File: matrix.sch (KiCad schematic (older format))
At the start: 135 parts

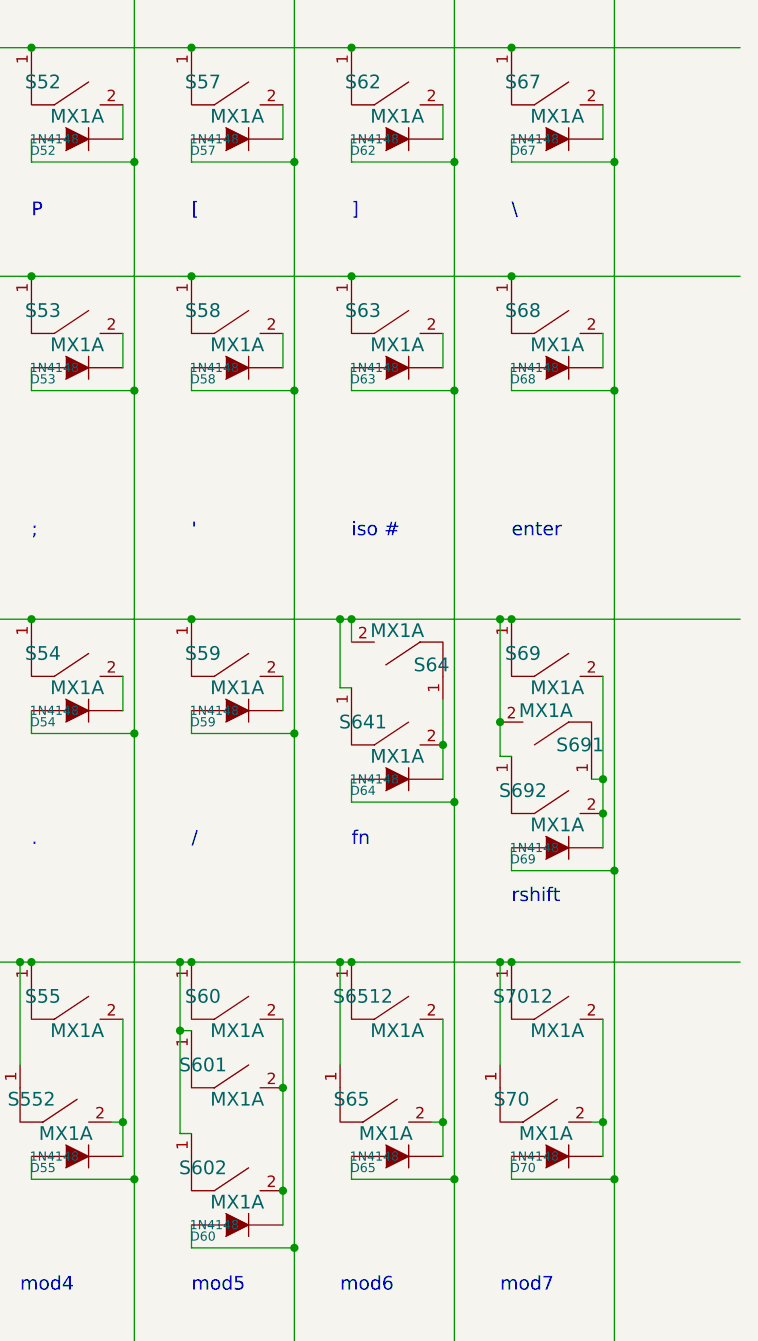
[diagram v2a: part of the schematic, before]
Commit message: Remove old layout around rswitch
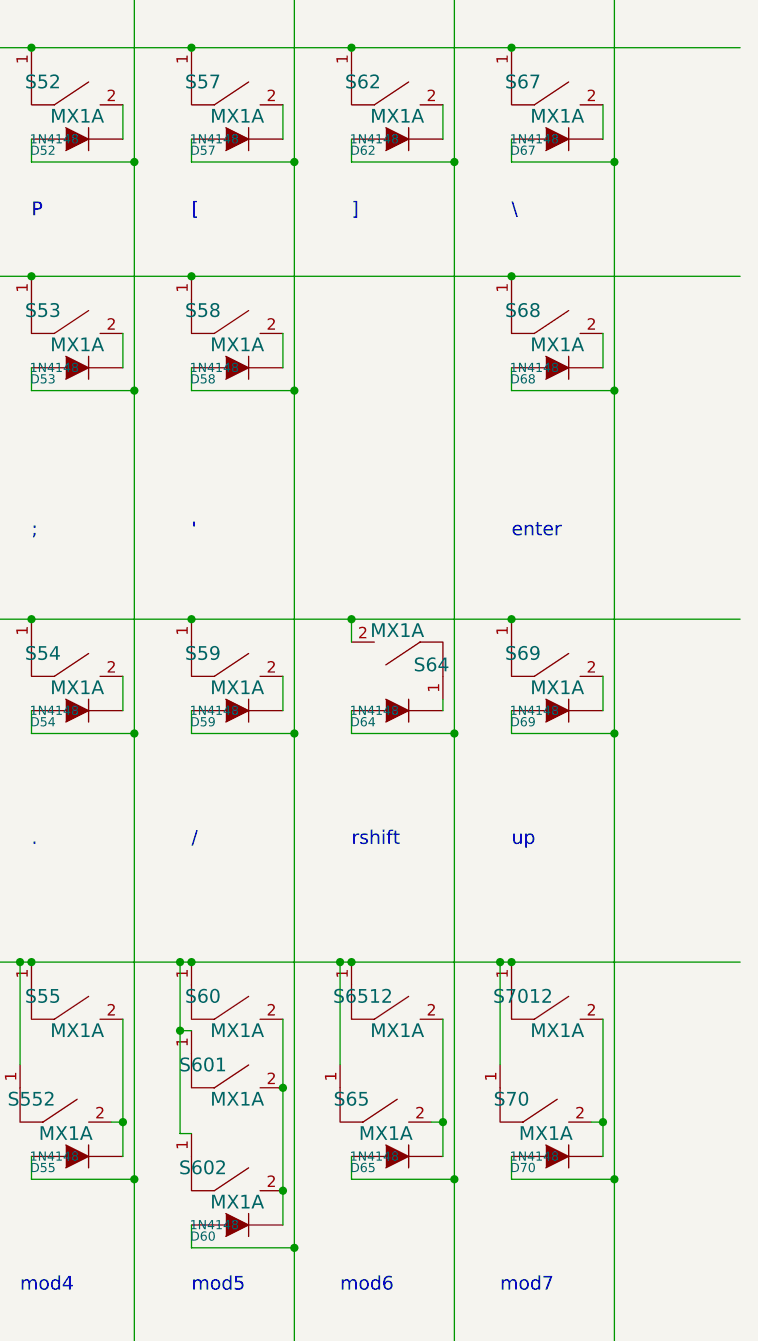
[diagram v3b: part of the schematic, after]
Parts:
- removed D63: 1N4148, 0805:0805D, symbol device:DIODE
- removed S63, S641, S691, S692: MX1A, mx1a:MX1A_no3d, symbol mx1a-simple:MX1A
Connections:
- wire segments 370 -> 354
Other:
- note added: "up"
- note removed: "fn"
- note removed: "iso #"
- moved on the sheet: D64, D69
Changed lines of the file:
@@
-$EndComp
-$Comp
-L mx1a-simple:MX1A S63
-U 1 1 5040DE9F
-P 11750 5550
-F 0 "S63" H 11600 5800 60  0000 C CNN
-F 1 "MX1A" H 11750 5650 60  0000 C CNN
-F 2 "mx1a:MX1A_no3d" H 11750 5550 60  0001 C CNN
-F 3 "" H 11750 5550 60  0001 C CNN
-	1    11750 5550
-	1    0    0    -1
 $EndComp
 $Comp
@@
 F 3 "" H 12400 9000 60  0001 C CNN
 	1    12400 9000
-	1    0    0    -1
-$EndComp
-$Comp
-L mx1a-simple:MX1A S641
-U 1 1 5040E2D0
-P 11750 7350
-F 0 "S641" H 11600 7600 60  0000 C CNN
-F 1 "MX1A" H 11750 7450 60  0000 C CNN
-F 2 "mx1a:MX1A_no3d" H 11750 7350 60  0001 C CNN
-F 3 "" H 11750 7350 60  0001 C CNN
-	1    11750 7350
 	1    0    0    -1
 $EndComp
@@
 $EndComp
 $Comp
-L mx1a-simple:MX1A S691
-U 1 1 5051FE50
-P 12400 6950
-F 0 "S691" H 12250 7200 60  0000 C CNN
-F 1 "MX1A" H 12400 7050 60  0000 C CNN
-F 2 "mx1a:MX1A_no3d" H 12400 6950 60  0001 C CNN
-F 3 "" H 12400 6950 60  0001 C CNN
-	1    12400 6950
-	-1   0    0    1
-$EndComp
-$Comp
-L mx1a-simple:MX1A S692
-U 1 1 5051FE56
-P 12450 7650
-F 0 "S692" H 12300 7900 60  0000 C CNN
-F 1 "MX1A" H 12450 7750 60  0000 C CNN
-F 2 "mx1a:MX1A_no3d" H 12450 7650 60  0001 C CNN
-F 3 "" H 12450 7650 60  0001 C CNN
-	1    12450 7650
-	1    0    0    -1
-$EndComp
-$Comp
 L device:DIODE D06
 U 1 1 506B1C22
@@
 L device:DIODE D64
 U 1 1 506B59D7
-P 11750 7350
-F 0 "D64" H 11600 7300 40  0000 C CNN
-F 1 "1N4148" H 11650 7350 40  0000 C CNN
-F 2 "0805:0805D" H 11750 7350 60  0001 C CNN
-F 3 "" H 11750 7350 60  0001 C CNN
-F 4 "DC Components" H 5150 4750 60  0001 C CNN "Vendor"
-F 5 "CD4148WS(0805C)" H 5150 4750 60  0001 C CNN "Product"
-F 6 "TME" H 5150 4750 60  0001 C CNN "Supplier"
-F 7 "1N4148-0805" H 5150 4750 60  0001 C CNN "Supplier Symbol"
-	1    11750 7350
+P 11750 7050
+F 0 "D64" H 11600 7000 40  0000 C CNN
+F 1 "1N4148" H 11650 7050 40  0000 C CNN
+F 2 "0805:0805D" H 11750 7050 60  0001 C CNN
+F 3 "" H 11750 7050 60  0001 C CNN
+F 4 "DC Components" H 5150 4450 60  0001 C CNN "Vendor"
+F 5 "CD4148WS(0805C)" H 5150 4450 60  0001 C CNN "Product"
+F 6 "TME" H 5150 4450 60  0001 C CNN "Supplier"
+F 7 "1N4148-0805" H 5150 4450 60  0001 C CNN "Supplier Symbol"
+	1    11750 7050
 	1    0    0    -1
 $EndComp
@@
 L device:DIODE D69
 U 1 1 506B59E0
-P 12450 7650
-F 0 "D69" H 12300 7600 40  0000 C CNN
-F 1 "1N4148" H 12350 7650 40  0000 C CNN
-F 2 "0805:0805D" H 12450 7650 60  0001 C CNN
-F 3 "" H 12450 7650 60  0001 C CNN
-F 4 "DC Components" H 5300 4750 60  0001 C CNN "Vendor"
-F 5 "CD4148WS(0805C)" H 5300 4750 60  0001 C CNN "Product"
-F 6 "TME" H 5300 4750 60  0001 C CNN "Supplier"
-F 7 "1N4148-0805" H 5300 4750 60  0001 C CNN "Supplier Symbol"
-	1    12450 7650
+P 12450 7050
+F 0 "D69" H 12300 7000 40  0000 C CNN
+F 1 "1N4148" H 12350 7050 40  0000 C CNN
+F 2 "0805:0805D" H 12450 7050 60  0001 C CNN
+F 3 "" H 12450 7050 60  0001 C CNN
+F 4 "DC Components" H 5300 4150 60  0001 C CNN "Vendor"
+F 5 "CD4148WS(0805C)" H 5300 4150 60  0001 C CNN "Product"
+F 6 "TME" H 5300 4150 60  0001 C CNN "Supplier"
+F 7 "1N4148-0805" H 5300 4150 60  0001 C CNN "Supplier Symbol"
+	1    12450 7050
 	1    0    0    -1
 $EndComp
@@
 F 7 "1N4148-0805" H 5300 4050 60  0001 C CNN "Supplier Symbol"
 	1    12450 5550
-	1    0    0    -1
-$EndComp
-$Comp
-L device:DIODE D63
-U 1 1 506B5A1F
-P 11750 5550
-F 0 "D63" H 11600 5500 40  0000 C CNN
-F 1 "1N4148" H 11650 5550 40  0000 C CNN
-F 2 "0805:0805D" H 11750 5550 60  0001 C CNN
-F 3 "" H 11750 5550 60  0001 C CNN
-F 4 "DC Components" H 5150 4350 60  0001 C CNN "Vendor"
-F 5 "CD4148WS(0805C)" H 5150 4350 60  0001 C CNN "Product"
-F 6 "TME" H 5150 4350 60  0001 C CNN "Supplier"
-F 7 "1N4148-0805" H 5150 4350 60  0001 C CNN "Supplier Symbol"
-	1    11750 5550
 	1    0    0    -1
 $EndComp
@@
 Text Notes 10850 6300 0    60   ~ 0
 '
-Text Notes 11550 6300 0    60   ~ 0
-iso #
 Text Notes 12250 6300 0    60   ~ 0
 enter
@@
 /
 Text Notes 11550 7650 0    60   ~ 0
-fn
-Text Notes 12250 7900 0    60   ~ 0
 rshift
+Text Notes 12250 7650 0    60   ~ 0
+up
 Text Notes 3100 9600 0    60   ~ 0
 mod1
@@
 Connection ~ 10150 5150
 Connection ~ 10850 5150
-Connection ~ 11550 5150
 Connection ~ 12250 5150
 Connection ~ 12250 4150
@@
 	12000 1400 12000 3450
 Wire Wire Line
-	11500 6650 11500 6950
-Wire Wire Line
-	11500 6950 11550 6950
-Connection ~ 11500 6650
-Wire Wire Line
-	11950 7000 11950 7200
-Wire Wire Line
 	10550 8850 10500 8850
 Wire Wire Line
@@
 	12650 8850 12600 8850
 Wire Wire Line
-	12200 6650 12200 7100
-Connection ~ 12200 6650
-Wire Wire Line
-	12200 7250 12250 7250
-Wire Wire Line
-	12650 6900 12650 7350
+	12650 6900 12650 7050
 Wire Wire Line
 	3850 3350 3850 3450
@@
 	11250 7050 11250 6900
 Wire Wire Line
-	11550 7350 11550 7450
-Wire Wire Line
-	11550 7450 12000 7450
-Wire Wire Line
-	12250 7650 12250 7750
-Wire Wire Line
-	12250 7750 12700 7750
+	11550 7050 11550 7150
+Wire Wire Line
+	11550 7150 12000 7150
+Wire Wire Line
+	12250 7050 12250 7150
+Wire Wire Line
+	12250 7150 12700 7150
 Wire Wire Line
 	12250 9000 12250 9100
@@
 Wire Wire Line
 	12250 5650 12700 5650
-Wire Wire Line
-	11550 5550 11550 5650
-Wire Wire Line
-	11550 5650 12000 5650
-Wire Wire Line
-	11950 5550 11950 5400
 Wire Wire Line
 	10850 5550 10850 5650
@@
 Connection ~ 10600 5650
 Connection ~ 11300 5650
-Connection ~ 12000 5650
 Connection ~ 12700 9100
-Connection ~ 12700 7750
-Connection ~ 12000 7450
 Connection ~ 12000 9100
 Connection ~ 11300 9400
@@
 Connection ~ 9900 7150
 Connection ~ 9200 7150
-Connection ~ 11950 7200
 Connection ~ 9450 5150
 Connection ~ 9450 4150
 Connection ~ 9450 2950
-Connection ~ 12650 7500
 Wire Wire Line
 	11550 6750 11550 6650
@@
 	12250 3450 12250 3350
 Wire Wire Line
-	12600 7350 12650 7350
-Connection ~ 12650 7350
-Connection ~ 12200 7100
-Wire Wire Line
 	10100 8150 10150 8150
 Wire Wire Line
@@
 	12250 6650 13250 6650
 Wire Wire Line
-	10850 6650 11500 6650
-Wire Wire Line
-	11550 6650 12200 6650
-Wire Wire Line
 	10150 6650 10850 6650
 Wire Wire Line
@@
 	10150 5150 10850 5150
 Wire Wire Line
-	10850 5150 11550 5150
-Wire Wire Line
 	12250 5150 13250 5150
 Wire Wire Line
@@
 	11250 8700 11250 9150
 Wire Wire Line
-	11500 6650 11550 6650
-Wire Wire Line
-	12200 6650 12250 6650
-Wire Wire Line
 	5250 2950 5950 2950
 Wire Wire Line
@@
 	12700 4650 12700 5650
 Wire Wire Line
-	12000 4650 12000 5650
-Wire Wire Line
 	11300 4650 11300 5650
 Wire Wire Line
@@
 	11300 5650 11300 7150
 Wire Wire Line
-	12000 5650 12000 7450
-Wire Wire Line
 	12700 9100 12700 10000
 Wire Wire Line
-	12700 7750 12700 9100
-Wire Wire Line
-	12000 7450 12000 9100
-Wire Wire Line
 	12000 9100 12000 10000
 Wire Wire Line
@@
 	9200 7150 9200 10000
 Wire Wire Line
-	11950 7200 11950 7350
-Wire Wire Line
 	9450 5150 10150 5150
 Wire Wire Line
@@
 Wire Wire Line
 	9450 2950 10150 2950
-Wire Wire Line
-	12650 7500 12650 7650
-Wire Wire Line
-	12650 7350 12650 7500
-Wire Wire Line
-	12200 7100 12200 7250
 Wire Wire Line
 	9900 7150 9900 10000
@@
 Wire Wire Line
 	12650 5400 12650 5550
-Wire Wire Line
-	11550 5150 12250 5150
 Connection ~ 12700 5650
 Wire Wire Line
-	12700 5650 12700 7750
+	12700 5650 12700 7150
 Wire Wire Line
 	12250 5550 12250 5650
+Wire Wire Line
+	11950 7000 11950 7050
+Wire Wire Line
+	10850 6650 11550 6650
+Connection ~ 12000 7150
+Wire Wire Line
+	12000 7150 12000 9100
+Wire Wire Line
+	11550 6650 12250 6650
+Connection ~ 12700 7150
+Wire Wire Line
+	12700 7150 12700 9100
+Wire Wire Line
+	10850 5150 12250 5150
+Wire Wire Line
+	12000 4650 12000 7150
 $EndSCHEMATC

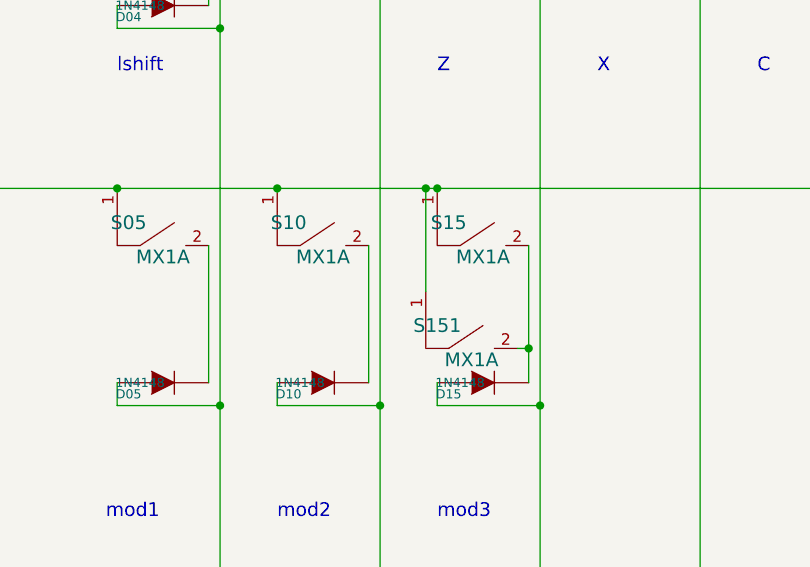
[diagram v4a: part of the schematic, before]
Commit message: Remove leds from PCB
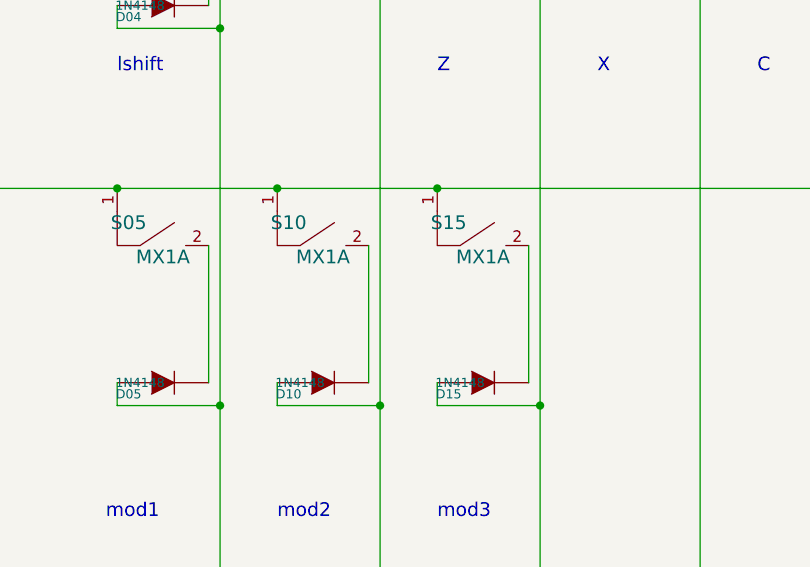
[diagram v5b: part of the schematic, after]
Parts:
- removed S151: MX1A, mx1a:MX1A_no3d, symbol mx1a-simple:MX1A
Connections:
- wire segments 354 -> 350
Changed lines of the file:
@@
 	4300 9100 4300 10000
-Wire Wire Line
-	4950 8850 4950 9000
-Wire Wire Line
-	4950 8400 4950 8850
-Connection ~ 4950 8850
-Wire Wire Line
-	4950 8850 4900 8850
-Wire Wire Line
-	3850 8150 4500 8150
-Wire Wire Line
-	4500 8150 4550 8150
-Connection ~ 4500 8150
-Wire Wire Line
-	4500 8150 4500 8600
-$Comp
-L mx1a-simple:MX1A S151
-U 1 1 5040F14F
-P 4700 9000
-F 0 "S151" H 4550 9250 60  0000 C CNN
-F 1 "MX1A" H 4700 9100 60  0000 C CNN
-F 2 "mx1a:MX1A_no3d" H 4700 9000 60  0001 C CNN
-F 3 "" H 4700 9000 60  0001 C CNN
-	1    4700 9000
-	1    0    0    -1
-$EndComp
 Wire Wire Line
 	1800 5150 3150 5150
@@
 Wire Wire Line
 	12000 4650 12000 7150
+Wire Wire Line
+	3850 8150 4550 8150
+Wire Wire Line
+	4950 8400 4950 9000
 $EndSCHEMATC

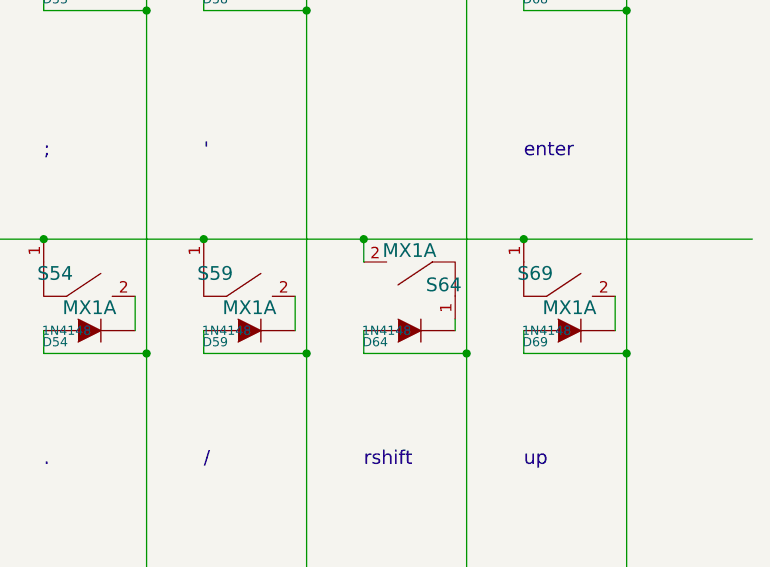
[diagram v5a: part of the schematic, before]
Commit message: Add rswitch and up buttons
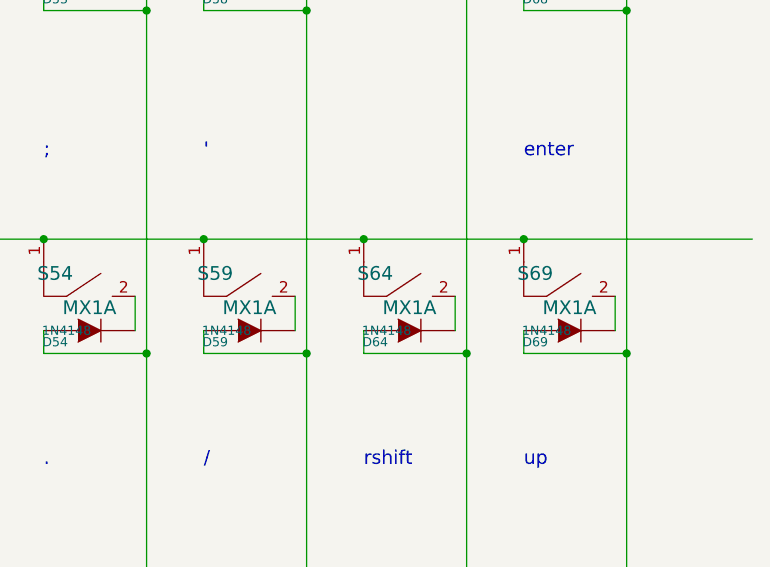
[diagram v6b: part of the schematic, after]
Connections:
- wire segments 350 -> 349
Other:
- moved on the sheet: S64
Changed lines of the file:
@@
-$EndComp
-$Comp
-L mx1a-simple:MX1A S64
-U 1 1 5040DEFF
-P 11750 6600
-F 0 "S64" H 11600 6850 60  0000 C CNN
-F 1 "MX1A" H 11750 6700 60  0000 C CNN
-F 2 "mx1a:MX1A_no3d" H 11750 6600 60  0001 C CNN
-F 3 "" H 11750 6600 60  0001 C CNN
-	1    11750 6600
-	-1   0    0    1
 $EndComp
 $Comp
@@
 Connection ~ 12250 6650
 Connection ~ 10850 6650
-Connection ~ 11550 6650
 Connection ~ 10150 6650
 Connection ~ 6650 6650
@@
 Connection ~ 9450 2950
 Wire Wire Line
-	11550 6750 11550 6650
-Wire Wire Line
 	10800 8900 10850 8900
 Wire Wire Line
@@
 Wire Wire Line
 	12250 5550 12250 5650
-Wire Wire Line
-	11950 7000 11950 7050
+Connection ~ 12000 7150
+Wire Wire Line
+	12000 7150 12000 9100
+Connection ~ 12700 7150
+Wire Wire Line
+	12700 7150 12700 9100
+Wire Wire Line
+	10850 5150 12250 5150
+Wire Wire Line
+	12000 4650 12000 7150
+Wire Wire Line
+	3850 8150 4550 8150
+Wire Wire Line
+	4950 8400 4950 9000
 Wire Wire Line
 	10850 6650 11550 6650
-Connection ~ 12000 7150
-Wire Wire Line
-	12000 7150 12000 9100
+$Comp
+L mx1a-simple:MX1A S64
+U 1 1 5040DEFF
+P 11750 7050
+F 0 "S64" H 11600 7300 60  0000 C CNN
+F 1 "MX1A" H 11750 7150 60  0000 C CNN
+F 2 "mx1a:MX1A_no3d" H 11750 7050 60  0001 C CNN
+F 3 "" H 11750 7050 60  0001 C CNN
+	1    11750 7050
+	1    0    0    -1
+$EndComp
+Connection ~ 11550 6650
 Wire Wire Line
 	11550 6650 12250 6650
-Connection ~ 12700 7150
-Wire Wire Line
-	12700 7150 12700 9100
-Wire Wire Line
-	10850 5150 12250 5150
-Wire Wire Line
-	12000 4650 12000 7150
-Wire Wire Line
-	3850 8150 4550 8150
-Wire Wire Line
-	4950 8400 4950 9000
+Wire Wire Line
+	11950 6900 11950 7050
 $EndSCHEMATC
